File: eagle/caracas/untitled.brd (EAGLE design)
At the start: 110.2 x 53.3 mm, 26 parts, among them IC1 4027N, Q1 IRLZ44Z, X1 22-23-2021, X2 22-23-2021, X3 22-23-2041, X4 22-23-2041, X5 22-23-2021, X6 22-23-2021

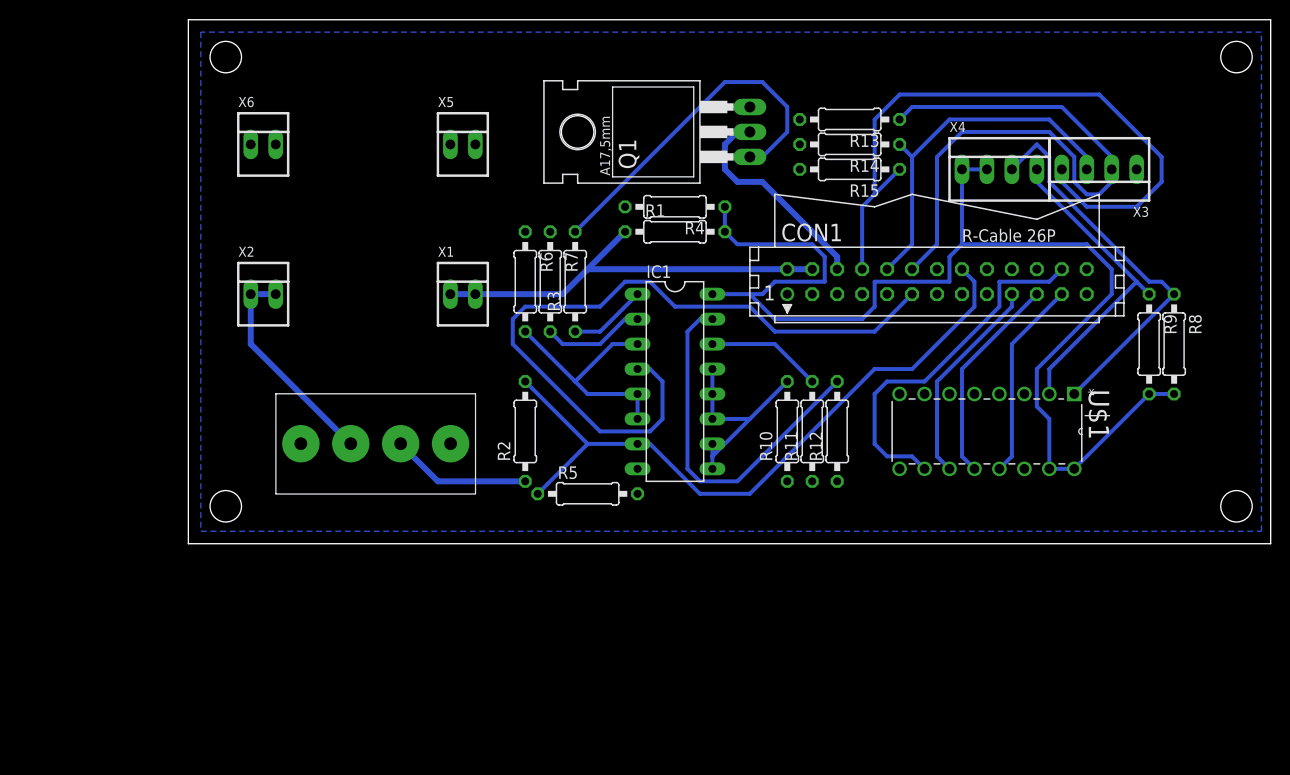
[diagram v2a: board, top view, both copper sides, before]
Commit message: Schematics: replace CD4027N J/K flip-flop with 4011N nand gates.
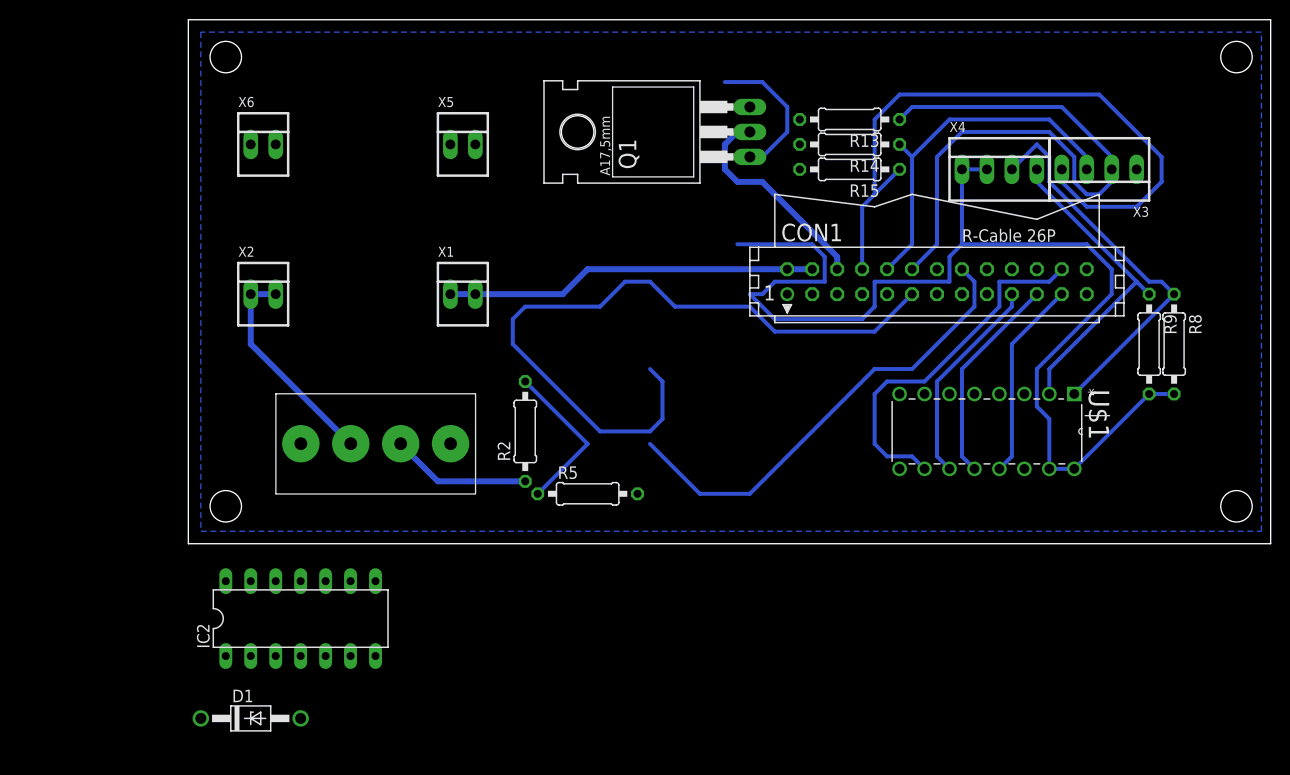
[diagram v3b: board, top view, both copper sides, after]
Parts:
- removed IC1: 4027N, 40xx:DIL16
- removed R1, R10, R11, R12, R3, R4, R6, R7: (no value), rcl:0207/10
- added D1: 1N4728, diode:DO41Z10
- added IC2: 4011N, 40xx:DIL14
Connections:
- removed net N$11: IC1.14, R11.2
- removed net N$12: IC1.10, IC1.11, IC1.12, IC1.13, IC1.9, R10.2
- removed net N$13: IC1.15, R12.2
- removed net N$14: IC1.1, R3.1
- removed net N$2: IC1.2, R7.2
- removed net N$9: IC1.3, IC1.5, IC1.6, R6.2
- removed net SUICIDE: CON1.11, IC1.4
- new net N$16: IC2.2, IC2.4
- new net RPI_RESET: CON1.11, IC2.6
- new net RPI_SET: IC2.1
- net +3.3V: now also CON1.1; no longer IC1.16, R1.2, R4.1
- net +5V: now also IC2.14; no longer R1.1
- net GND: now also D1.A, IC2.7; no longer IC1.8, R10.1, R11.1, R12.1, R4.2, R6.1, R7.1
- net N$1: now also IC2.3, IC2.5; no longer R3.2
- net POWER_STATE: now also D1.C; no longer IC1.7
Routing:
- net SUICIDE: track 74.8 -> 0.00 mm
- net RPI_RESET: track 0.00 -> 73.5 mm
- net N$13: track 37.0 -> 0.00 mm
- net N$9: track 24.5 -> 0.00 mm
- net N$12: track 22.2 -> 0.00 mm
- net N$1: track 36.4 -> 14.8 mm
- net N$11: track 11.7 -> 0.00 mm
- net N$2: track 10.5 -> 0.00 mm
- net +3.3V: track 123.3 -> 115.2 mm
- net N$14: track 7.93 -> 0.00 mm
- net POWER_STATE: track 69.9 -> 63.5 mm
- net +5V: track 43.3 -> 37.9 mm

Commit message: Remove obsolete component from electronics schematics. Clean up board paths.
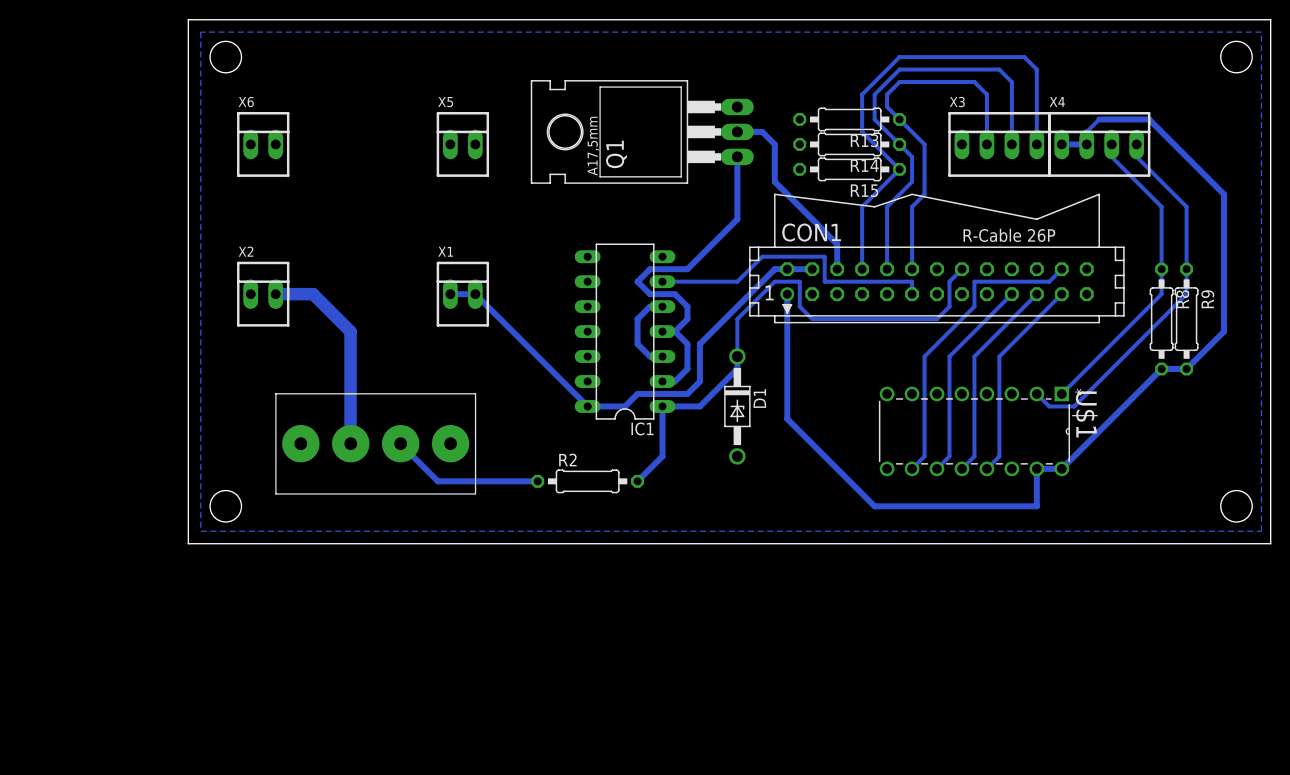
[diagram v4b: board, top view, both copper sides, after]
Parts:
- removed IC2: 4011N, 40xx:DIL14
- removed R5: (no value), rcl:0207/10
- added IC1: 4001N, 40xx:DIL14
- moved D1 58.8 mm to (55.9, 14.0), turned to 270 degrees
- moved X3 10.5 mm to (82.5, 40.6), turned to 0 degrees
- moved X4 10.5 mm to (92.7, 40.6)
- moved R2 8.13 mm to (40.6, 6.35), turned to 0 degrees
- moved R9 4.58 mm to (101.6, 22.9)
- moved R8 2.84 mm to (99.1, 22.9)
- moved Q1 1.27 mm to (49.5, 41.9)
- moved U$1 1.27 mm to (71.1, 7.62)
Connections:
- removed net N$16: IC2.2, IC2.4
- removed net RPI_SET: IC2.1
- new net MOSFET_ON: IC1.2, IC1.4, Q1.G
- net +5V: now also IC1.14; no longer IC2.14
- net GND: now also IC1.7, X3.1; no longer IC2.7, R5.2
- net N$1: now also IC1.3, IC1.5; no longer IC2.3, IC2.5, Q1.G
- net POWER_STATE: now also IC1.1; no longer R5.1
- net RPI_RESET: now also IC1.6; no longer IC2.6
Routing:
- net RPI_RESET: track 73.5 -> 30.3 mm
- net MOSFET_ON: track 0.00 -> 37.0 mm
- net N$10: track 62.7 -> 36.2 mm
- net N$7: track 68.3 -> 48.4 mm
- net +5V: track 37.9 -> 49.6 mm
- net POWER_STATE: track 63.5 -> 54.0 mm
- net +3.3V: track 115.2 -> 105.9 mm
- net ANA_0: track 39.7 -> 31.7 mm
- net N$1: track 14.8 -> 8.67 mm
- net N$6: track 37.0 -> 31.1 mm
- net N$8: track 36.5 -> 42.3 mm
- net ANA_1: track 32.5 -> 37.8 mm
- net +5V_SW_GND: track 22.0 -> 19.7 mm
- net VCC: track 22.0 -> 20.6 mm
- net +12V_IGN: track 14.3 -> 15.6 mm
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
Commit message: Use correct size for DC/DC converter, and compress size of board.
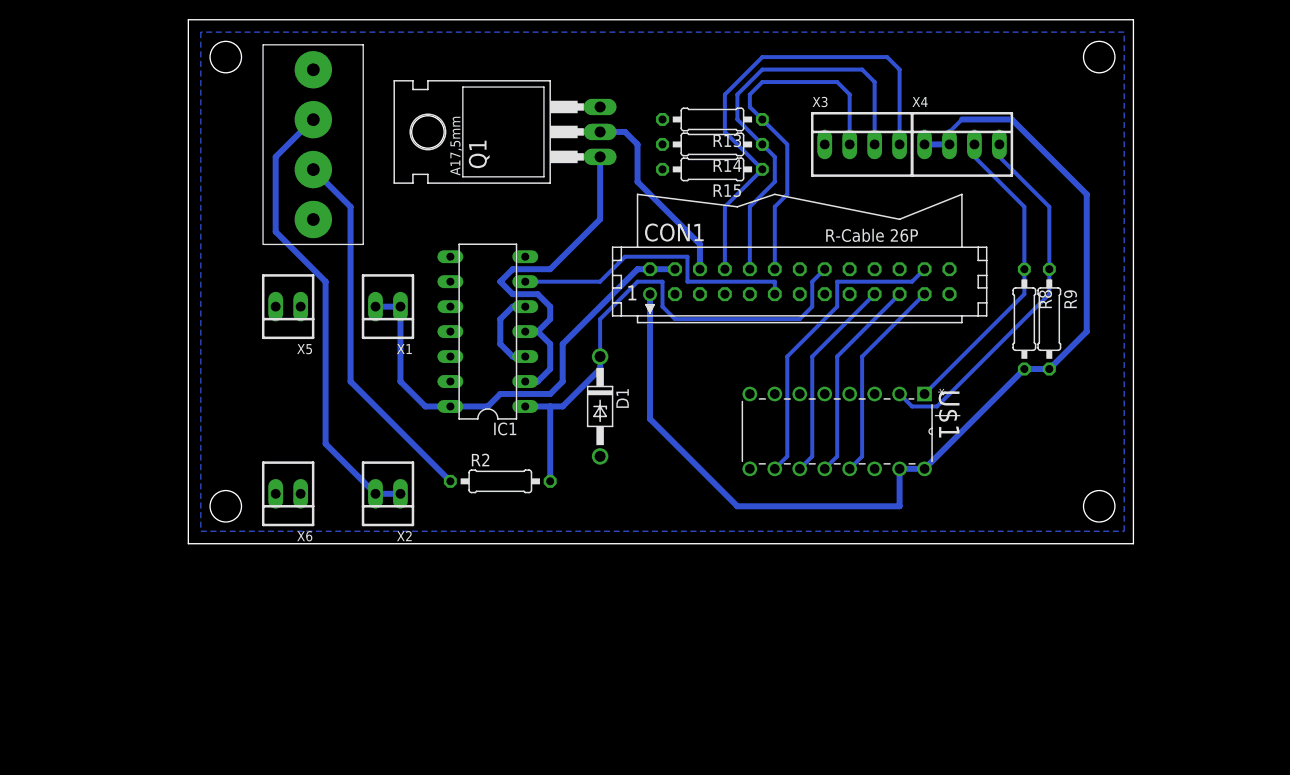
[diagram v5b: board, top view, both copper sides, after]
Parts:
- moved X6 35.7 mm to (10.2, 5.08), turned to 180 degrees
- moved U$2 31.1 mm to (12.7, 40.6), turned to 270 degrees
- moved X5 24.3 mm to (10.2, 24.1), turned to 180 degrees
- moved X2 24.0 mm to (20.3, 5.08), turned to 180 degrees
- moved CON1 14.0 mm to (62.2, 26.7)
- moved D1 14.0 mm to (41.9, 14.0)
- moved U$1 14.0 mm to (57.1, 7.62)
- moved IC1 14.0 mm to (30.5, 21.6)
- moved Q1 14.0 mm to (35.6, 41.9)
- moved R13 14.0 mm to (53.3, 43.2)
- moved R14 14.0 mm to (53.3, 40.6)
- moved R15 14.0 mm to (53.3, 38.1)
- moved R8 14.0 mm to (85.1, 22.9)
- moved R9 14.0 mm to (87.6, 22.9)
- moved X3 14.0 mm to (68.6, 40.6)
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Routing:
- net VCC: track 20.6 -> 46.4 mm
- net +12V_IGN: track 15.6 -> 37.5 mm
- net +5V: track 49.6 -> 47.2 mm
- net POWER_STATE: track 54.0 -> 53.0 mm
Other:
- board size 110.2 x 53.3 mm -> 96.2 x 53.3 mm

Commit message: Update schematics again.
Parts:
- added R1, R3: (no value), rcl:0207/10
- added T1: (no value), transistor:TO92-CBE
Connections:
- new net N$2: IC1.6, R1.2, T1.C
- new net N$9: R3.1, T1.B
- net +12V_IGN: now also IC1.1
- net +5V: no longer IC1.14
- net GND: now also T1.E
- net MOSFET_ON: no longer Q1.G
- net N$1: now also Q1.G
- net POWER_STATE: no longer IC1.1
- net RPI_RESET: now also R3.2; no longer IC1.6
- net VCC: now also IC1.14, R1.1
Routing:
- net VCC: track 46.4 -> 82.5 mm
- net MOSFET_ON: track 37.0 -> 8.67 mm
- net N$1: track 8.67 -> 33.1 mm
- net +12V_IGN: track 37.5 -> 48.3 mm
- net RPI_RESET: track 30.3 -> 22.6 mm
- net +5V: track 47.2 -> 41.7 mm
- net +5V_SW_GND: track 19.7 -> 17.1 mm
- net POWER_STATE: track 53.0 -> 50.5 mm
- net +3.3V: track 105.9 -> 104.6 mm

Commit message: Assign values to resistors.
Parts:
- added R4: 10k, rcl:0207/10
- added R5: 1.2k, rcl:0207/10
- added T2: (no value), transistor:TO92-CBE
- R1: value (none) -> 10k
- R3: value (none) -> 260
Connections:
- new net N$11: IC1.1, R4.2, T2.C
- new net N$12: R5.2, T2.B
- net +12V_IGN: now also R5.1; no longer IC1.1
- net GND: now also T2.E
- net VCC: now also R4.1
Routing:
- net +12V_IGN: track 48.3 -> 37.5 mm
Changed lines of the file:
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@@
 <element name="D1" library="diode" package="DO41Z10" value="1N4728" x="41.91" y="13.97" rot="R270"/>
 <element name="IC1" library="40xx" package="DIL14" value="4001N" x="30.48" y="21.59" rot="R90"/>
-<element name="R1" library="rcl" package="0207/10" value="" x="6.35" y="-5.08"/>
+<element name="R1" library="rcl" package="0207/10" value="10k" x="6.35" y="-5.08"/>
 <element name="T1" library="transistor" package="TO92-CBE" value="" x="-5.08" y="-1.27"/>
-<element name="R3" library="rcl" package="0207/10" value="" x="-2.54" y="-10.16"/>
+<element name="R3" library="rcl" package="0207/10" value="260" x="-2.54" y="-10.16"/>
+<element name="R4" library="rcl" package="0207/10" value="10k" x="-2.54" y="-15.24"/>
+<element name="T2" library="transistor" package="TO92-CBE" value="" x="-13.97" y="-11.43"/>
+<element name="R5" library="rcl" package="0207/10" value="1.2k" x="-11.43" y="-20.32"/>
 </elements>
 <signals>
@@
 <contactref element="T1" pad="E"/>
 <contactref element="Q1" pad="S"/>
+<contactref element="T2" pad="E"/>
+<wire x1="-2.54" y1="-1.27" x2="-11.43" y2="-11.43" width="0" layer="19" extent="1-1"/>
 <wire x1="8.89" y1="5.08" x2="-2.54" y2="-1.27" width="0" layer="19" extent="1-1"/>
 </signal>
@@
 <wire x1="16.51" y1="34.29" x2="16.51" y2="16.51" width="0.6096" layer="16"/>
 <wire x1="16.51" y1="16.51" x2="26.67" y2="6.35" width="0.6096" layer="16"/>
-<contactref element="IC1" pad="1"/>
 <contactref element="U$2" pad="P$4"/>
-<wire x1="26.67" y1="6.35" x2="34.29" y2="13.97" width="0.6096" layer="16"/>
 <wire x1="16.51" y1="34.29" x2="12.72" y2="38.08" width="0.6096" layer="16"/>
+<contactref element="R5" pad="1"/>
+<wire x1="16.51" y1="16.51" x2="-16.51" y2="-20.32" width="0" layer="19" extent="16-16"/>
 </signal>
 <signal name="+5V" class="2">
@@
 <wire x1="8.89" y1="39.33" x2="12.72" y2="43.16" width="0.6096" layer="16"/>
 <contactref element="R1" pad="1"/>
+<contactref element="R4" pad="1"/>
 <wire x1="1.27" y1="-5.08" x2="19.05" y2="5.08" width="0" layer="19" extent="1-1"/>
+<wire x1="-7.62" y1="-15.24" x2="1.27" y2="-5.08" width="0" layer="19" extent="1-1"/>
 </signal>
 <signal name="N$2">
@@
 <wire x1="-5.08" y1="-1.27" x2="-7.62" y2="-10.16" width="0" layer="19" extent="1-1"/>
 </signal>
+<signal name="N$11">
+<contactref element="IC1" pad="1"/>
+<contactref element="R4" pad="2"/>
+<contactref element="T2" pad="C"/>
+<wire x1="2.54" y1="-15.24" x2="34.29" y2="13.97" width="0" layer="19" extent="1-1"/>
+<wire x1="-16.51" y1="-11.43" x2="2.54" y2="-15.24" width="0" layer="19" extent="1-1"/>
+</signal>
+<signal name="N$12">
+<contactref element="R5" pad="2"/>
+<contactref element="T2" pad="B"/>
+<wire x1="-13.97" y1="-11.43" x2="-6.35" y2="-20.32" width="0" layer="19" extent="1-1"/>
+</signal>
 </signals>

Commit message: WIP schematics
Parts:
- removed CON1: (no value), con-harting:CON26
- removed R13, R14, R15: (no value), rcl:0207/10
- removed U$2: MKDS3, caracas:MKDS3
- added MCP3008: MCP3008-I/P, mpc3008:DIP254P762X432-16
- added R10: 1k, rcl:0207/10
- added R6, R7: 330, rcl:0207/10
- added RASPBERRYPI: (no value), con-harting:CON26
- R1: value 10k -> 870
- R2: value (none) -> 1.2k
- R3: value 260 -> 10k
- R5: value 1.2k -> 260
- R8: value (none) -> 330
- R9: value (none) -> 1k
- U$1: value MCP3008-I/P -> MKDS3; device mpc3008:DIP254P762X432-16 -> caracas:MKDS3
- X3: value 22-23-2041 -> 22-23-2021; device con-molex:22-23-2041 -> con-molex:22-23-2021
- X6: value 22-23-2021 -> 22-23-2041; device con-molex:22-23-2021 -> con-molex:22-23-2041
- moved X6 78.4 mm to (80.0, 40.6), turned to 0 degrees
- moved R5 72.9 mm to (36.8, 34.3)
- moved X3 68.4 mm to (10.2, 5.08), turned to 180 degrees
- moved T2 57.5 mm to (27.9, 27.9), turned to 180 degrees
- moved U$1 55.4 mm to (12.7, 40.6)
- moved T1 40.2 mm to (27.9, 21.6), turned to 180 degrees
- moved R4 39.7 mm to (27.9, 10.2), turned to 90 degrees
- moved R3 38.8 mm to (30.5, 10.2), turned to 90 degrees
- moved R1 37.0 mm to (40.6, 8.89)
- moved R8 36.6 mm to (54.6, 43.2), turned to 180 degrees
- moved D1 10.9 mm to (52.1, 10.2)
- moved X1 10.2 mm to (10.2, 24.1)
- moved X5 10.2 mm to (20.3, 24.1)
- moved X4 8.89 mm to (69.8, 40.6)
- moved IC1 7.73 mm to (38.1, 22.9)
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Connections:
- net +12V_IGN: now also R1.1, U$1.P$4; no longer R5.1, U$2.P$4
- net +3.3V: now also MCP3008.15, MCP3008.16, R10.2, RASPBERRYPI.1, X6.1, X6.2; no longer CON1.1, R8.2, U$1.15, U$1.16, X4.1, X4.2
- net +5V: now also RASPBERRYPI.2, RASPBERRYPI.4, X5.1, X5.2; no longer CON1.2, CON1.4, X1.1, X1.2
- net +5V_SW_GND: now also RASPBERRYPI.6; no longer CON1.6
- net ANA_0: now also MCP3008.1, R10.1, X6.3; no longer R8.1, U$1.1, X4.3
- net ANA_1: now also MCP3008.2, X6.4; no longer U$1.2, X4.4
- net GND: now also MCP3008.14, MCP3008.9, R6.2, R7.2, R8.2, U$1.P$1, X1.1, X1.2, X3.2, X4.1; no longer R13.2, R14.2, R15.2, U$1.14, U$1.9, U$2.P$1, X5.1, X5.2, X6.1, X6.2
- net N$10: now also R8.1, RASPBERRYPI.12, X4.2; no longer CON1.12, R13.1, X3.2
- net N$11: now also R3.2, T1.C; no longer R4.2, T2.C
- net N$12: now also R2.2, T1.B; no longer R5.2, T2.B
- net N$2: now also R4.2, T2.C; no longer R1.2, T1.C
- net N$3: now also MCP3008.13, RASPBERRYPI.23; no longer CON1.23, U$1.13
- net N$4: now also MCP3008.12, RASPBERRYPI.21; no longer CON1.21, U$1.12
- net N$5: now also MCP3008.11, RASPBERRYPI.19; no longer CON1.19, U$1.11
- net N$6: now also MCP3008.10, RASPBERRYPI.24; no longer CON1.24, U$1.10
- net N$7: now also R6.1, RASPBERRYPI.8, X4.4; no longer CON1.8, R15.1, X3.4
- net N$8: now also R7.1, RASPBERRYPI.10, X4.3; no longer CON1.10, R14.1, X3.3
- net N$9: now also R5.1, T2.B; no longer R3.1, T1.B
- net POWER_STATE: now also R1.2, RASPBERRYPI.16; no longer CON1.16, R2.2
- net RPI_RESET: now also R5.2, RASPBERRYPI.11; no longer CON1.11, R3.2
- net VCC: now also R3.1, U$1.P$3; no longer R1.1, U$2.P$3
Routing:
- net N$1: track 33.1 -> 85.5 mm
- net N$2: track 0.00 -> 26.8 mm
- net N$11: track 0.00 -> 18.8 mm
- net +12V_IGN: track 37.5 -> 52.9 mm
- net N$9: track 0.00 -> 7.93 mm
- net N$12: track 0.00 -> 7.40 mm
- net +3.3V: track 104.6 -> 97.7 mm
- net VCC: track 82.5 -> 77.6 mm
- net +5V: track 41.7 -> 45.6 mm
- net +5V_SW_GND: track 17.1 -> 20.9 mm
- net RPI_RESET: track 22.6 -> 25.0 mm
- net POWER_STATE: track 50.5 -> 48.2 mm
- net ANA_1: track 37.8 -> 36.8 mm
- net ANA_0: track 31.7 -> 30.7 mm
- net N$7: track 48.4 -> 47.7 mm
